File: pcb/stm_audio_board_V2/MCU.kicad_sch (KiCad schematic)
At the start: 11 parts, among them J2 STlink, J5 SPI, SW1 SW_SPST, U1 STM32H730VBTx, Y2 X1E0000210132

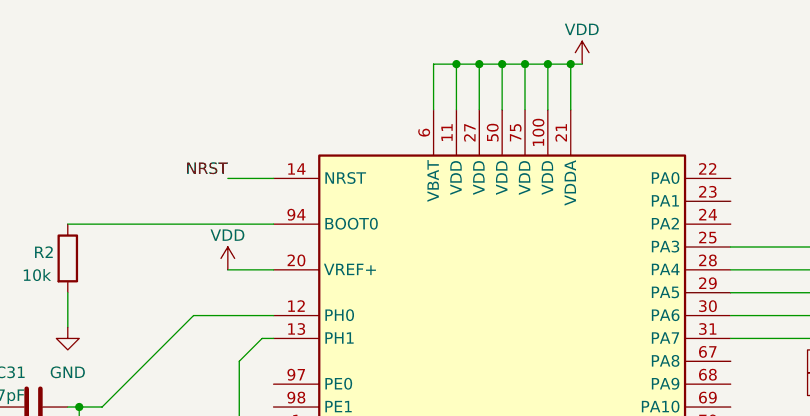
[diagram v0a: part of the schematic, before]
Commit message: ad1939 symbol is finished
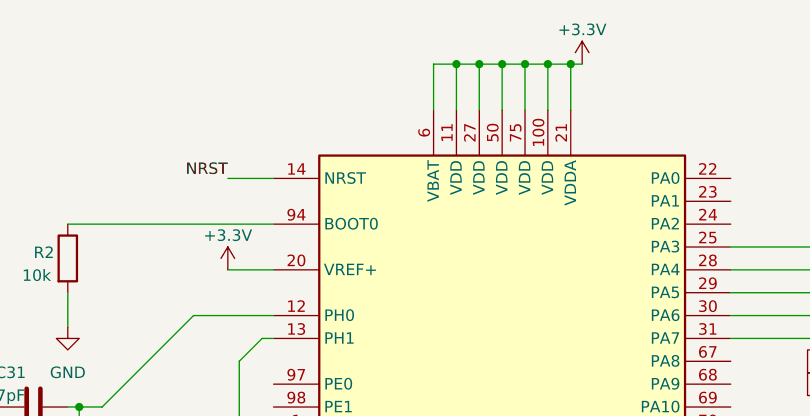
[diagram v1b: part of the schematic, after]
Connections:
- net VDD is gone; now on net +3.3V: U1.100 (VDD), U1.11 (VDD), U1.20 (VREF+), U1.21 (VDDA), U1.27 (VDD), U1.50 (VDD), U1.6 (VBAT), U1.75 (VDD)

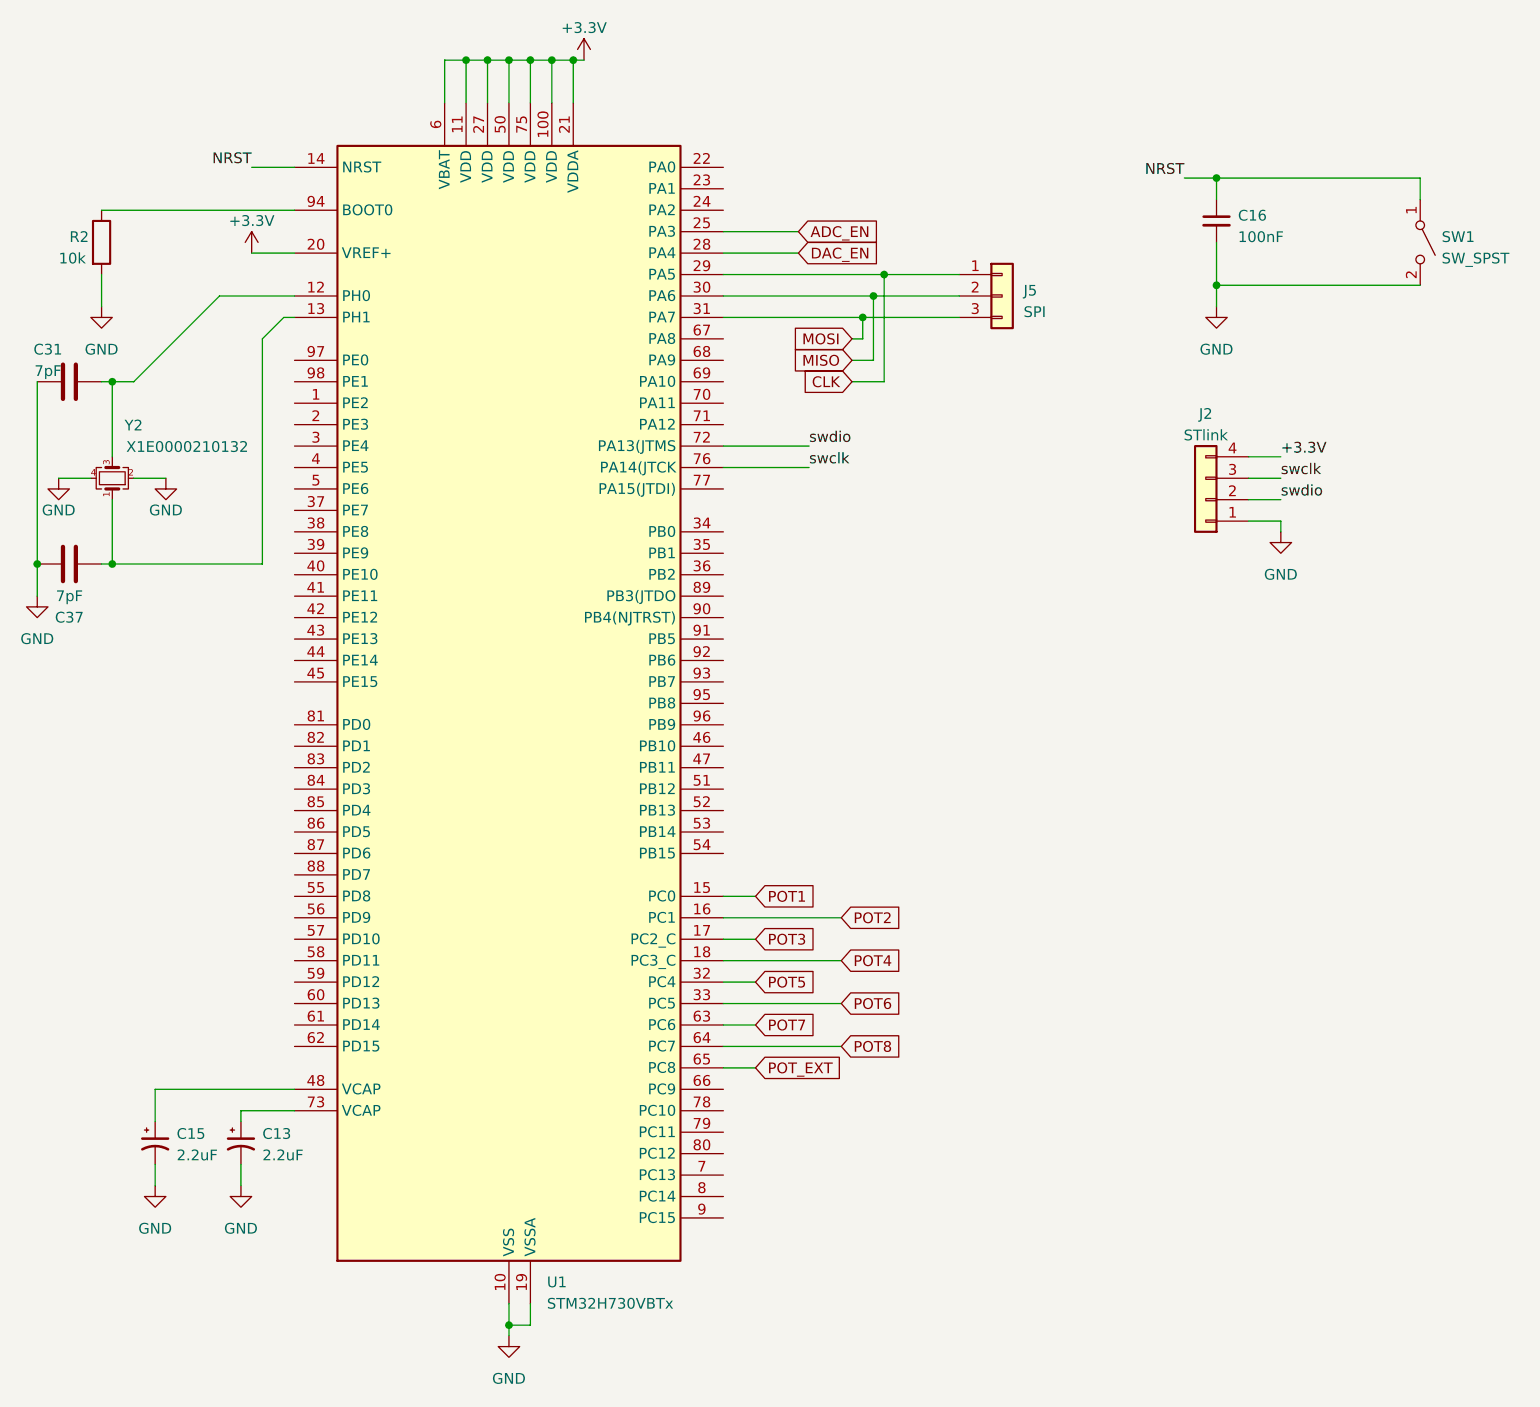
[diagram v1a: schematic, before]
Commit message: input and output stage reworked in sim and in schematic, power filtering is changed, further calculations needed
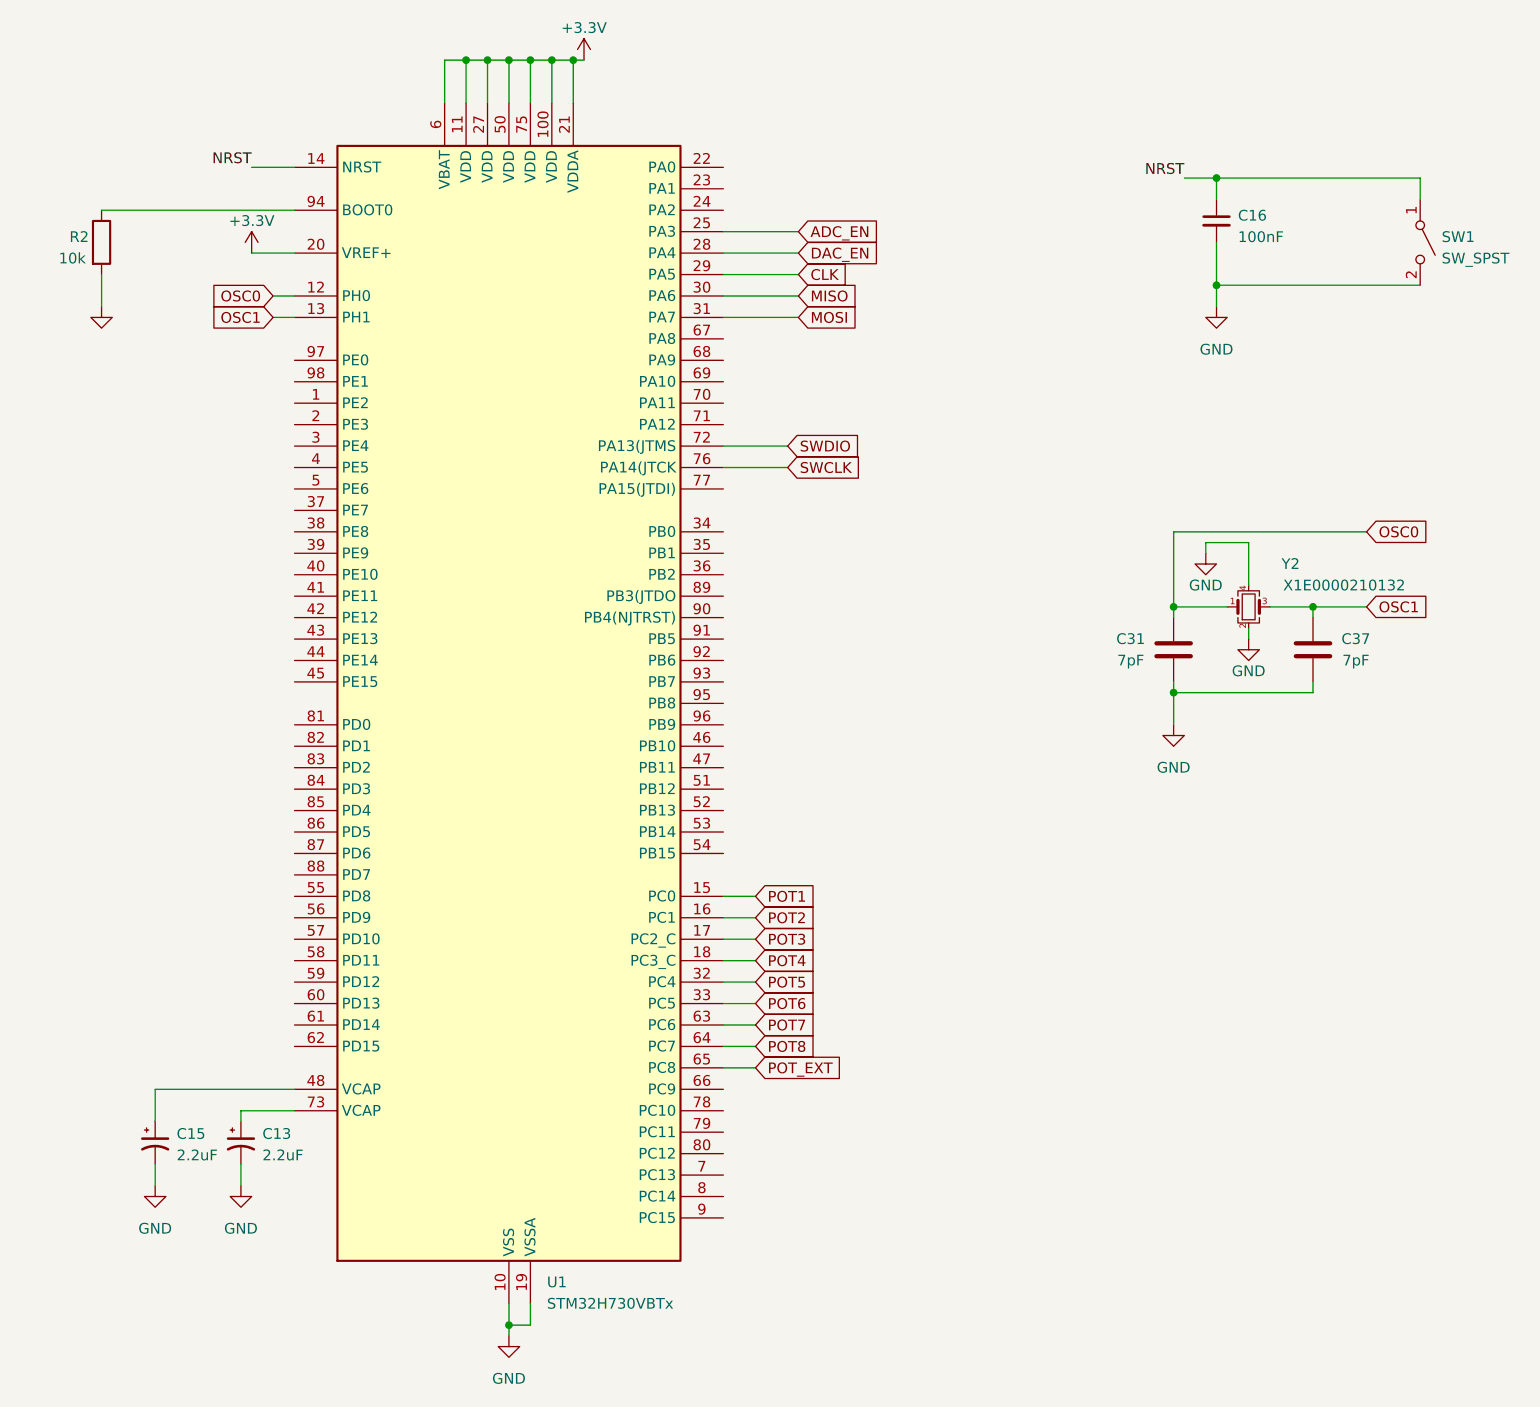
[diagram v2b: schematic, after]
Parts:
- removed J2: STlink, Connector_PinHeader_2.54mm:PinHeader_1x04_P2.54mm_Vertical, symbol Connector_Generic:Conn_01x04
- removed J5: SPI, Connector_PinHeader_2.54mm:PinHeader_1x03_P2.54mm_Vertical, symbol Connector_Generic:Conn_01x03
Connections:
- net OSC1: now reaches C37.2, U1.13 (PH1)
- net OSC1: now also Y2.3; no longer Y2.1
- net OSC0: now reaches C31.2, U1.12 (PH0)
- net OSC0: now also Y2.1; no longer Y2.3
- net swclk renamed SWCLK
- net swdio renamed SWDIO
